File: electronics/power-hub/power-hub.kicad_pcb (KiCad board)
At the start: 2 copper layers, 120 x 70 mm, 74 parts, among them J1 24V IN, J2 ROW A, J3 ROW B, J4 ROW C, J5 ROW D, J6 ROW AUX, J7 SUPERVISOR, Q1 SUD50P06-15, U1 TPS26600PWPR, U2 TPS26600PWPR, U3 TPS26600PWPR, U4 TPS26600PWPR, U5 TPS26600PWPR

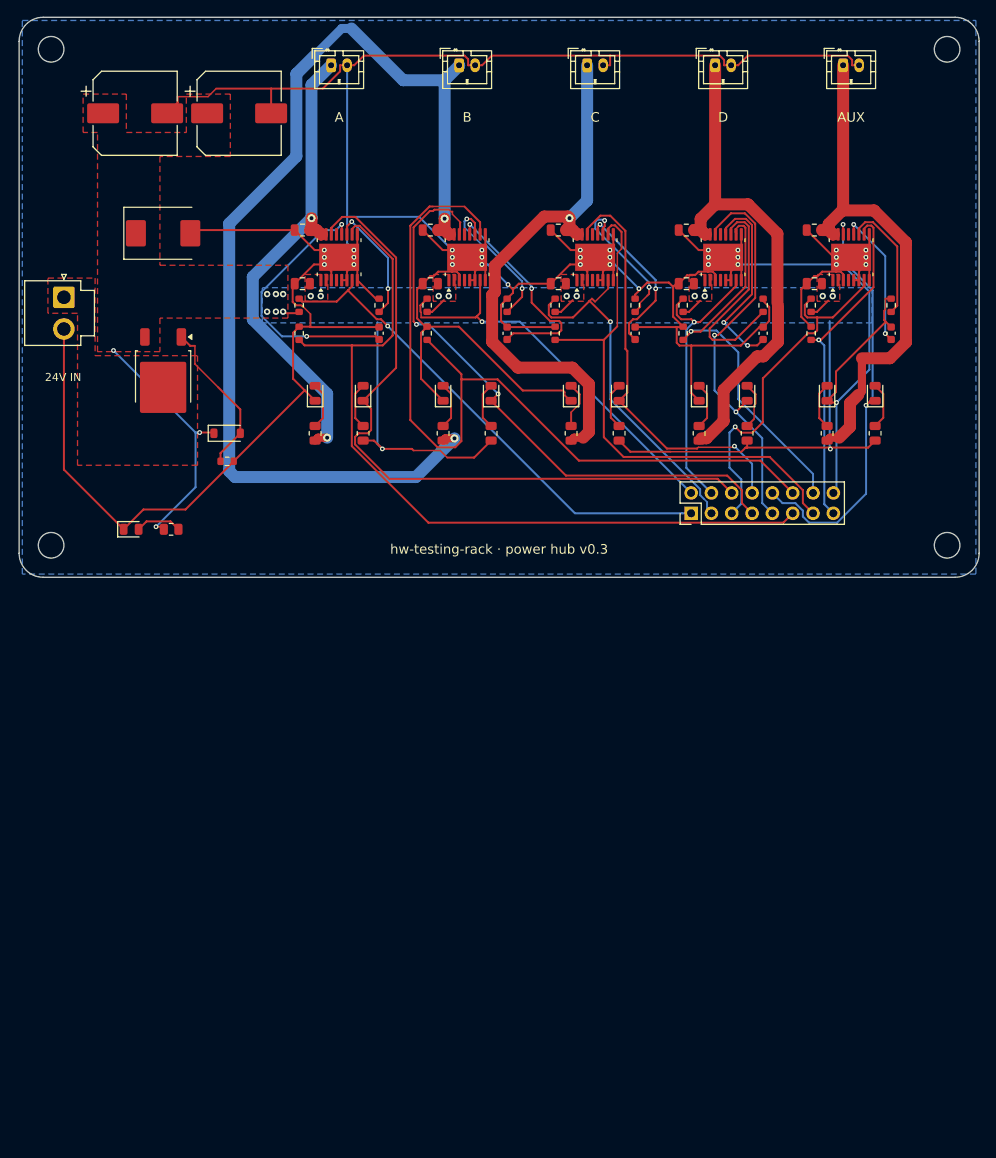
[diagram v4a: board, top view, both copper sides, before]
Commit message: Power hub v0.4: eFuses + rack controller (ESP32-S3, CAN master)
A new board for the power box: 76 x 140 mm, 2 layers, drawn around the
outline, holes, row connectors and front LEDs in config/rack.yaml.

- 24 V in on a JST VH (the brick's crimped DC cord), P-FET + TVS + bulk,
  then 4 x TPS26600 (1.6 A) to 6-pin JST PH row outputs: 24 V, GND,
  CAN_H, CAN_L, GND, POS (docs/can.md)
- every row on without firmware (SHDN held high by a 1M/150k divider from
  24 V); the controller can switch a row off (2N7002) and reads FLT and IMON
- rack controller: ESP32-S3-MINI-1, LMR51635 5 V buck (the bay node's
  layout) diode-ORed with USB-C VBUS, AMS1117; TCAN1044AV with both
  terminations of the star bus (2 x 56 ohm split, twice), PESD2CAN; POS per
  row through 10k + BAT54S clamp (survives a reversed cable)
- side-view ON / FAULT LEDs per row, 24V and CTL in the box's front wall
- autorouted; ERC 0, DRC 0, 0 unconnected, parity 0; Konnect review in
  docs/review-konnect.md (VBUS cap added; the rest per-sheet false positives)
- box re-generated for the final hole / connector / LED positions; viewer
  shows the real board; BOM carries an estimate (Standard PCBA, not quoted)
- schematic: automatic block layout for now

Co-Authored-By: Claude Opus 5.5 <noreply@anthropic.com>
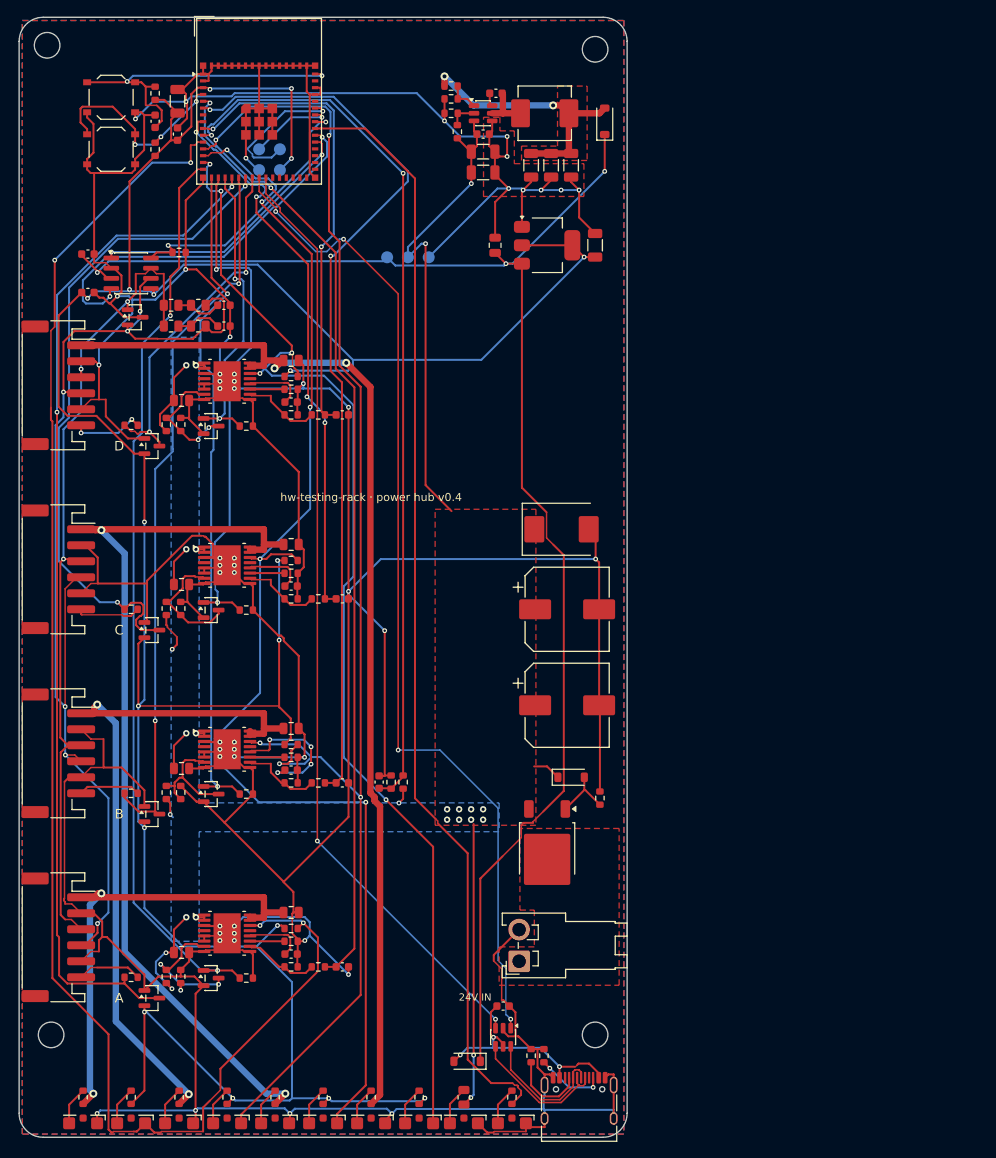
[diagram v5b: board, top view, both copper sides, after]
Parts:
- removed C15, C35: 1u, Capacitor_SMD:C_0805_2012Metric
- removed C25: 22n, Capacitor_SMD:C_0603_1608Metric
- removed D15: ON, LED_SMD:LED_0805_2012Metric
- removed D25: FAULT, LED_SMD:LED_0805_2012Metric
- removed J7: SUPERVISOR, Connector_PinHeader_2.54mm:PinHeader_2x08_P2.54mm_Vertical
- removed R15: 470k, Resistor_SMD:R_0603_1608Metric
- removed R25: 7.5k, Resistor_SMD:R_0603_1608Metric
- removed R35: 18k, Resistor_SMD:R_0603_1608Metric
- removed R45, R55: 10k, Resistor_SMD:R_0805_2012Metric
- removed U1: TPS26600PWPR, Package_SO:HTSSOP-16-1EP_4.4x5mm_P0.65mm_EP3.4x5mm_Mask2.66x2.46mm
- added C104: 10u, Capacitor_SMD:C_1206_3216Metric, F.Cu at (58.0, 16.8)
- added C105: 10u, Capacitor_SMD:C_1206_3216Metric, F.Cu at (58.0, 19.4)
- added C106: 100n, Capacitor_SMD:C_0603_1608Metric, F.Cu at (58.0, 14.6)
- added C107: 100n, Capacitor_SMD:C_0603_1608Metric, F.Cu at (59.6, 9.50)
- added C108: 22u, Capacitor_SMD:C_1206_3216Metric, F.Cu at (64.0, 18.5)
- added C109: 22u, Capacitor_SMD:C_1206_3216Metric, F.Cu at (66.5, 18.5)
- added C110: 22u, Capacitor_SMD:C_1206_3216Metric, F.Cu at (69.0, 18.5)
- added C111: 10u, Capacitor_SMD:C_0805_2012Metric, F.Cu at (59.5, 28.5)
- added C112: 22u, Capacitor_SMD:C_1206_3216Metric, F.Cu at (72.0, 28.5)
- added C113: 22u, Capacitor_SMD:C_1206_3216Metric, F.Cu at (19.8, 10.5)
- added C114: 100n, Capacitor_SMD:C_0603_1608Metric, F.Cu at (19.8, 14.6)
- added C115: 1u, Capacitor_SMD:C_0603_1608Metric, F.Cu at (17.0, 13.0)
- added C116: 100n, Capacitor_SMD:C_0603_1608Metric, F.Cu at (8.60, 29.6)
- added C117: 100n, Capacitor_SMD:C_0603_1608Metric, F.Cu at (8.60, 34.4)
- added C118: 4.7n, Capacitor_SMD:C_0603_1608Metric, F.Cu at (25.6, 36.0)
- added C119: 4.7n, Capacitor_SMD:C_0603_1608Metric, F.Cu at (25.6, 38.6)
- added C120: 1u, Capacitor_SMD:C_0603_1608Metric, F.Cu at (60.5, 123.6)
- added C3: 100n, Capacitor_SMD:C_0603_1608Metric, F.Cu at (45.0, 95.6)
- added C61: 10n, Capacitor_SMD:C_0603_1608Metric, F.Cu at (40.4, 118.7)
- added C62: 10n, Capacitor_SMD:C_0603_1608Metric, F.Cu at (40.4, 95.7)
- added C63: 10n, Capacitor_SMD:C_0603_1608Metric, F.Cu at (40.4, 72.7)
- added C64: 10n, Capacitor_SMD:C_0603_1608Metric, F.Cu at (40.4, 49.7)
- added D31: BAT54S, Package_TO_SOT_SMD:SOT-23, F.Cu at (16.6, 122.6)
- added D32: BAT54S, Package_TO_SOT_SMD:SOT-23, F.Cu at (16.6, 99.6)
- added D33: BAT54S, Package_TO_SOT_SMD:SOT-23, F.Cu at (16.6, 76.6)
- added D34: BAT54S, Package_TO_SOT_SMD:SOT-23, F.Cu at (16.6, 53.6)
- added D4: B5819W SL, Diode_SMD:D_SOD-123, F.Cu at (73.2, 13.0)
- added D5: B5819W SL, Diode_SMD:D_SOD-123, F.Cu at (56.0, 130.5)
- added D8: CTL, LED_SMD:LED_Kingbright_KPA-3010_3x2x1mm, F.Cu at (61.6, 138.8)
- added D9: PESD2CAN,215, Package_TO_SOT_SMD:SOT-23, F.Cu at (14.5, 37.5)
- added L1: 3.3u, Inductor_SMD:L_Changjiang_FXL0630, F.Cu at (65.7, 12.0)
- added Q2: 2N7002, Package_TO_SOT_SMD:SOT-23, F.Cu at (24.0, 120.1)
- added Q3: 2N7002, Package_TO_SOT_SMD:SOT-23, F.Cu at (24.0, 97.1)
- added Q4: 2N7002, Package_TO_SOT_SMD:SOT-23, F.Cu at (24.0, 74.1)
- added Q5: 2N7002, Package_TO_SOT_SMD:SOT-23, F.Cu at (24.0, 51.1)
- added R101: 10k, Resistor_SMD:R_0603_1608Metric, F.Cu at (14.0, 120.0)
- added R102: 10k, Resistor_SMD:R_0603_1608Metric, F.Cu at (14.0, 97.0)
- added R103: 10k, Resistor_SMD:R_0603_1608Metric, F.Cu at (14.0, 74.0)
- added R104: 10k, Resistor_SMD:R_0603_1608Metric, F.Cu at (14.0, 51.0)
- added R205: 1M, Resistor_SMD:R_0603_1608Metric, F.Cu at (54.8, 14.3)
- added R206: 100k, Resistor_SMD:R_0603_1608Metric, F.Cu at (54.0, 12.0)
- added R207: 120k, Resistor_SMD:R_0603_1608Metric, F.Cu at (54.0, 8.60)
- added R208: 22k, Resistor_SMD:R_0603_1608Metric, F.Cu at (54.0, 10.2)
- added R209: 10k, Resistor_SMD:R_0603_1608Metric, F.Cu at (17.0, 9.50)
- added R210: 10k, Resistor_SMD:R_0603_1608Metric, F.Cu at (17.0, 16.5)
- added R211: 330, Resistor_SMD:R_0603_1608Metric, F.Cu at (61.6, 135.0)
- added R212: 5.1k, Resistor_SMD:R_0603_1608Metric, F.Cu at (64.0, 129.8)
- added R213: 5.1k, Resistor_SMD:R_0603_1608Metric, F.Cu at (65.6, 129.8)
- added R214: 10k, Resistor_SMD:R_0603_1608Metric, F.Cu at (20.0, 29.4)
- added R215: 62, Resistor_SMD:R_0805_2012Metric, F.Cu at (19.0, 36.0)
- added R216: 62, Resistor_SMD:R_0805_2012Metric, F.Cu at (22.4, 36.0)
- added R217: 62, Resistor_SMD:R_0805_2012Metric, F.Cu at (19.0, 38.6)
- added R218: 62, Resistor_SMD:R_0805_2012Metric, F.Cu at (22.4, 38.6)
- added R3: 100k, Resistor_SMD:R_0603_1608Metric, F.Cu at (48.0, 95.6)
- added R4: 10k, Resistor_SMD:R_0603_1608Metric, F.Cu at (46.5, 95.6)
- added R61: 1k, Resistor_SMD:R_0603_1608Metric, F.Cu at (37.4, 118.7)
- added R62: 1k, Resistor_SMD:R_0603_1608Metric, F.Cu at (37.4, 95.7)
- added R63: 1k, Resistor_SMD:R_0603_1608Metric, F.Cu at (37.4, 72.7)
- added R64: 1k, Resistor_SMD:R_0603_1608Metric, F.Cu at (37.4, 49.7)
- added R71: 150k, Resistor_SMD:R_0603_1608Metric, F.Cu at (20.2, 119.9)
- added R72: 150k, Resistor_SMD:R_0603_1608Metric, F.Cu at (20.2, 96.9)
- added R73: 150k, Resistor_SMD:R_0603_1608Metric, F.Cu at (20.2, 73.9)
- added R74: 150k, Resistor_SMD:R_0603_1608Metric, F.Cu at (20.2, 50.9)
- added R81: 100k, Resistor_SMD:R_0603_1608Metric, F.Cu at (28.4, 120.1)
- added R82: 100k, Resistor_SMD:R_0603_1608Metric, F.Cu at (28.4, 97.1)
- added R83: 100k, Resistor_SMD:R_0603_1608Metric, F.Cu at (28.4, 74.1)
- added R84: 100k, Resistor_SMD:R_0603_1608Metric, F.Cu at (28.4, 51.1)
- added R91: 100k, Resistor_SMD:R_0603_1608Metric, F.Cu at (34.0, 113.9)
- added R92: 100k, Resistor_SMD:R_0603_1608Metric, F.Cu at (34.0, 90.9)
- added R93: 100k, Resistor_SMD:R_0603_1608Metric, F.Cu at (34.0, 67.9)
- added R94: 100k, Resistor_SMD:R_0603_1608Metric, F.Cu at (34.0, 44.9)
- added SW1: RESET, Button_Switch_SMD:SW_Push_1P1T_XKB_TS-1187A, F.Cu at (11.5, 10.0)
- added SW2: BOOT, Button_Switch_SMD:SW_Push_1P1T_XKB_TS-1187A, F.Cu at (11.5, 16.5)
- added TP1: U0TX, TestPoint:TestPoint_Pad_D1.5mm, B.Cu at (30.0, 16.5)
- added TP2: U0RX, TestPoint:TestPoint_Pad_D1.5mm, B.Cu at (32.6, 16.5)
- added TP3: GND, TestPoint:TestPoint_Pad_D1.5mm, B.Cu at (30.0, 19.1)
- added TP4: +3V3, TestPoint:TestPoint_Pad_D1.5mm, B.Cu at (32.6, 19.1)
- added TP5: +5V, TestPoint:TestPoint_Pad_D1.5mm, B.Cu at (46.0, 30.0)
- added TP6: +24V, TestPoint:TestPoint_Pad_D1.5mm, B.Cu at (48.6, 30.0)
- added TP7: GND, TestPoint:TestPoint_Pad_D1.5mm, B.Cu at (51.2, 30.0)
- added U11: TPS26600PWPR, Package_SO:HTSSOP-16-1EP_4.4x5mm_P0.65mm_EP3.4x5mm_Mask2.66x2.46mm, F.Cu at (26.0, 114.5)
- added U12: TPS26600PWPR, Package_SO:HTSSOP-16-1EP_4.4x5mm_P0.65mm_EP3.4x5mm_Mask2.66x2.46mm, F.Cu at (26.0, 91.5)
- added U13: TPS26600PWPR, Package_SO:HTSSOP-16-1EP_4.4x5mm_P0.65mm_EP3.4x5mm_Mask2.66x2.46mm, F.Cu at (26.0, 68.5)
- added U14: TPS26600PWPR, Package_SO:HTSSOP-16-1EP_4.4x5mm_P0.65mm_EP3.4x5mm_Mask2.66x2.46mm, F.Cu at (26.0, 45.5)
- added U6: TCAN1044AV, Package_SO:SOIC-8_3.9x4.9mm_P1.27mm, F.Cu at (14.0, 32.0)
- D11, D12, D13, D14, D21, D22, D23, D24, D3: footprint LED_SMD:LED_0805_2012Metric -> LED_SMD:LED_Kingbright_KPA-3010_3x2x1mm
- J1: footprint Connector_JST:JST_VH_B2P-VH_1x02_P3.96mm_Vertical -> Connector_JST:JST_VH_S2P-VH_1x02_P3.96mm_Horizontal
- J2, J3, J4, J5: footprint Connector_JST:JST_PH_B2B-PH-K_1x02_P2.00mm_Vertical -> Connector_JST:JST_PH_S6B-PH-SM4-TB_1x06-1MP_P2.00mm_Horizontal
- J6: value ROW AUX -> USB; footprint Connector_JST:JST_PH_B2B-PH-K_1x02_P2.00mm_Vertical -> Connector_USB:USB_C_Receptacle_HRO_TYPE-C-31-M-12
- R11, R12, R13, R14: value 470k -> 1M
- R41, R42, R43, R44: footprint Resistor_SMD:R_0805_2012Metric -> Resistor_SMD:R_0603_1608Metric
- R51, R52, R53, R54: value 10k -> 680; footprint Resistor_SMD:R_0805_2012Metric -> Resistor_SMD:R_0603_1608Metric
- U2: value TPS26600PWPR -> LMR51635YDDCR; footprint Package_SO:HTSSOP-16-1EP_4.4x5mm_P0.65mm_EP3.4x5mm_Mask2.66x2.46mm -> Package_TO_SOT_SMD:TSOT-23-6
- U3: value TPS26600PWPR -> AMS1117-3.3; footprint Package_SO:HTSSOP-16-1EP_4.4x5mm_P0.65mm_EP3.4x5mm_Mask2.66x2.46mm -> Package_TO_SOT_SMD:SOT-223-3_TabPin2
- U4: value TPS26600PWPR -> ESP32-S3-MINI-1-N8; footprint Package_SO:HTSSOP-16-1EP_4.4x5mm_P0.65mm_EP3.4x5mm_Mask2.66x2.46mm -> RF_Module:ESP32-S2-MINI-1
- U5: value TPS26600PWPR -> USBLC6-2SC6; footprint Package_SO:HTSSOP-16-1EP_4.4x5mm_P0.65mm_EP3.4x5mm_Mask2.66x2.46mm -> Package_TO_SOT_SMD:SOT-23-6
- moved J6 134.7 mm to (70.0, 136.6)
- moved J2 114.2 mm to (4.90, 115.0), turned to -90 degrees
- moved U5 106.8 mm to (60.5, 127.5), turned to -90 degrees
- moved J1 100.6 mm to (62.5, 118.0), turned to 90 degrees
- moved D14 100.5 mm to (44.0, 138.8), turned to 180 degrees
- moved D24 100.5 mm to (50.0, 138.8), turned to 180 degrees
- moved J3 99.5 mm to (4.90, 92.0), turned to -90 degrees
- moved D13 98.9 mm to (32.0, 138.8), turned to 180 degrees
- moved D23 98.9 mm to (38.0, 138.8), turned to 180 degrees
- moved D12 97.5 mm to (20.0, 138.8), turned to 180 degrees
- moved D22 97.5 mm to (26.0, 138.8), turned to 180 degrees
- moved D11 96.2 mm to (8.00, 138.8), turned to 180 degrees
- moved D21 96.2 mm to (14.0, 138.8), turned to 180 degrees
- moved R44 92.6 mm to (44.0, 135.0)
- moved R54 92.6 mm to (50.0, 135.0)
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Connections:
- R11 pad 2: SHDN_A -> /Outputs/SHDN_A
- R12 pad 2: SHDN_B -> /Outputs/SHDN_B
- R13 pad 2: SHDN_C -> /Outputs/SHDN_C
- R14 pad 2: SHDN_D -> /Outputs/SHDN_D
- R31 pad 1: IMON_A -> /Outputs/IMON_A
- R32 pad 1: IMON_B -> /Outputs/IMON_B
- R33 pad 1: IMON_C -> /Outputs/IMON_C
- R34 pad 1: IMON_D -> /Outputs/IMON_D
- R51 pad 1: +24V -> +3V3
- R52 pad 1: +24V -> +3V3
- R53 pad 1: +24V -> +3V3
- R54 pad 1: +24V -> +3V3
- U2 pad 1: +24V -> /Controller/BUCK_FB
- U2 pad 2: +24V -> /Controller/BUCK_EN
- U2 pad 3: GND -> +24V
- U2 pad 4: unconnected-(U2-NC-Pad4) -> GND
- U2 pad 5: GND -> /Controller/BUCK_SW
- U2 pad 6: GND -> /Controller/BUCK_CB
- U3 pad 1: +24V -> GND
- U3 pad 2: +24V -> +3V3
- U3 pad 3: GND -> +5V
- U4 pad 1: +24V -> GND
- U4 pad 10: IMON_D -> VSENSE
- U4 pad 11: /Outputs/ILIM_D -> FLT_A
- U4 pad 12: /Outputs/DVDT_D -> FLT_B
- U4 pad 13: unconnected-(U4-NC-Pad13) -> FLT_C
- U4 pad 15: /Outputs/ROW_D -> ROW_OFF_A
- U4 pad 16: /Outputs/ROW_D -> ROW_OFF_B
- U4 pad 17: GND -> ROW_OFF_C
- U4 pad 2: +24V -> GND
- U4 pad 3: GND -> +3V3
- U4 pad 4: unconnected-(U4-NC-Pad4) -> /Controller/BOOT
- U4 pad 5: GND -> ADC_IMON_A
- U4 pad 6: GND -> ADC_IMON_B
- U4 pad 7: SHDN_D -> unconnected-(U4-IO3-Pad7)
- U4 pad 8: GND -> ADC_IMON_C
- U4 pad 9: GND -> ADC_IMON_D
- U5 pad 1: +24V -> /Controller/USB_DN
- U5 pad 2: +24V -> GND
- U5 pad 3: GND -> /Controller/USB_DP
- U5 pad 4: unconnected-(U5-NC-Pad4) -> /Controller/USB_CONN_DP
- U5 pad 5: GND -> /Controller/VBUS
- U5 pad 6: GND -> /Controller/USB_CONN_DN
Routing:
- net +3V3: track 0.00 -> 391.1 mm, vias 0 -> 18
- net GND: track 551.6 -> 937.8 mm, vias 33 -> 51
- net +5V: track 0.00 -> 190.2 mm, vias 0 -> 3
- net CAN_L: track 0.00 -> 139.3 mm, vias 0 -> 6
- net /Controller/CTL_LED: track 0.00 -> 138.4 mm
- net POS_A: track 0.00 -> 128.2 mm, vias 0 -> 2
- net /Controller/USB_DN: track 0.00 -> 126.7 mm, vias 0 -> 4
- net ADC_IMON_A: track 0.00 -> 120.3 mm, vias 0 -> 2
- net /Controller/USB_DP: track 0.00 -> 118.2 mm, vias 0 -> 2
- net ROW_OFF_A: track 0.00 -> 114.6 mm, vias 0 -> 2
- net ADC_IMON_B: track 0.00 -> 113.2 mm, vias 0 -> 2
- net VSENSE: track 0.00 -> 110.9 mm, vias 0 -> 2
- net FLT_C: track 52.5 -> 160.6 mm, vias 1 -> 5
- net IMON_B: track 106.2 -> 0.00 mm
- net CAN_H: track 0.00 -> 104.8 mm, vias 0 -> 3
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- added copper zone on F.Cu, net /Controller/+5V_BUCK
- added copper zone on F.Cu, net GND
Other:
- board size 120 x 70 mm -> 76 x 140 mm
- board text added: "hw-testing-rack · power hub v0.4"
- board text removed: "AUX"
- board text removed: "hw-testing-rack · power hub v0.3"

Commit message: Power hub v0.5: USB-C PD input (AP33772S), 4 layers, rows off until enabled
The rack now runs from one USB PD 3.1 charger instead of the GST60A24 brick.

Hub v0.5 (76 x 140 mm, 4 layers, In1 GND, In2 VRACK/+3V3):
* AP33772S sink: 20 V at power-up (VSEL 39k), 28 V EPR on the controller's
  request, never 36/48 V; 5 mOhm Kelvin shunt, back-to-back IRF7842 switch,
  SMAJ30A TVS, NTC by the switch, interrupt and I2C to the ESP32-S3.
* USB4105 5 A receptacle; the controller's buck runs from VBUS (5-28 V),
  ahead of the switch.
* Every row's TPS26600 is off until the controller drives ROW_EN (SHDN pulled
  low); IMON per row; front PD LED.
* ERC 0, DRC 0 errors, 0 unconnected, parity 0; 146 3D models, 0 stand-ins.

Power box: 84 x 148 x 35 mm, hub only (no brick, no cradles), rear USB-C
cut-out, lid on corner lugs.  Viewer, BOM (charger + 5 A e-marked cable,
4-layer JLC estimate) and docs (power, mechanical, cabling, assembly,
electronics) follow.

Co-Authored-By: Claude Opus 5.5 <noreply@anthropic.com>
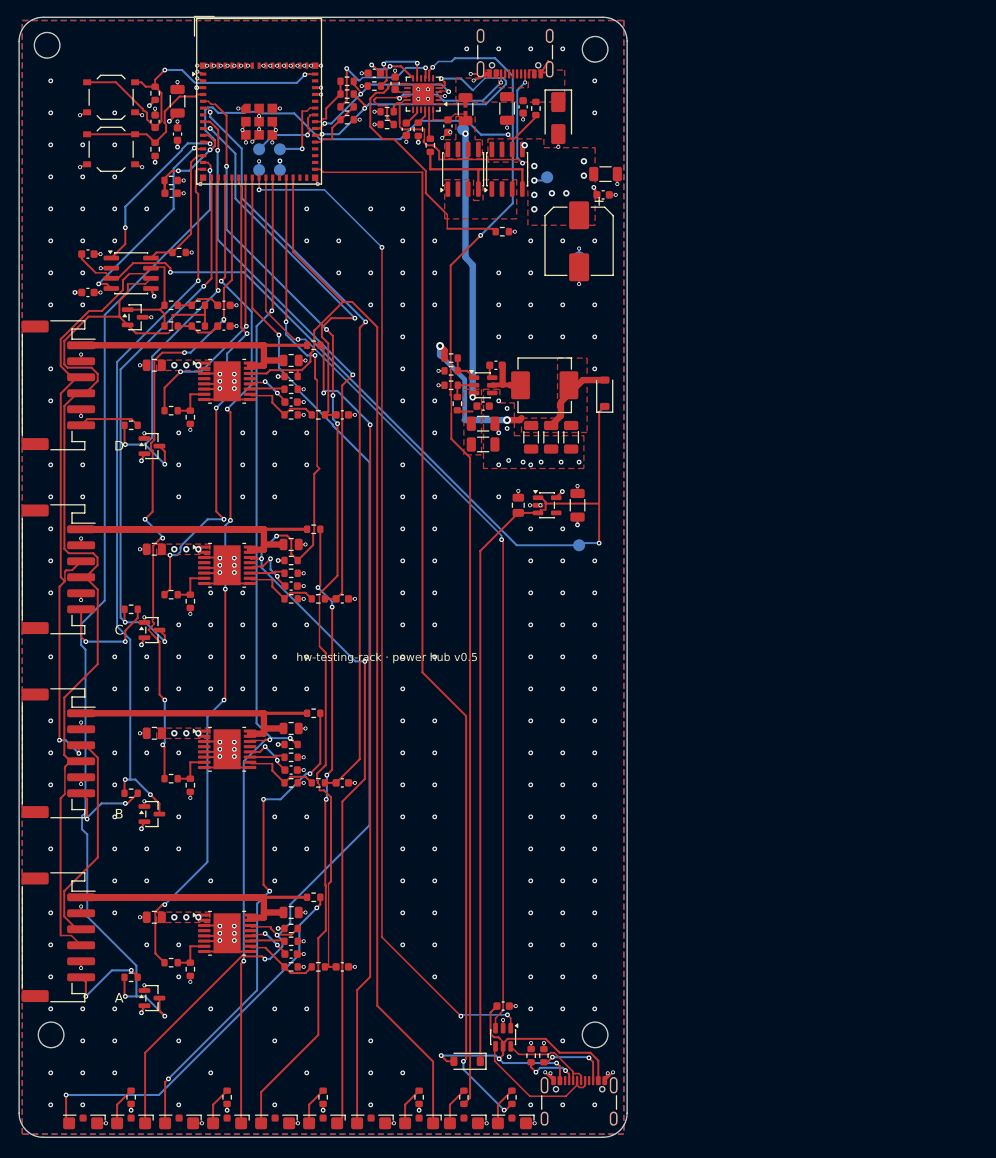
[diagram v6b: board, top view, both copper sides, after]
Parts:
- removed D2: SMCJ33A, Diode_SMD:D_SMC
- removed Q3, Q4, Q5: 2N7002, Package_TO_SOT_SMD:SOT-23
- added C10: 100n, Capacitor_SMD:C_0603_1608Metric, F.Cu at (73.0, 22.2)
- added C4: 1u, Capacitor_SMD:C_0603_1608Metric, F.Cu at (53.6, 13.6)
- added C5: 1u, Capacitor_SMD:C_0603_1608Metric, F.Cu at (48.4, 14.0)
- added C6: 100n, Capacitor_SMD:C_0603_1608Metric, F.Cu at (44.4, 7.00)
- added C7: 100n, Capacitor_SMD:C_0603_1608Metric, F.Cu at (47.0, 8.25)
- added C8: 100u/50V, Capacitor_SMD:CP_Elec_8x10, F.Cu at (70.0, 28.0)
- added C9: 10u, Capacitor_SMD:C_1206_3216Metric, F.Cu at (73.3, 19.6)
- added R5: 5.1k, Resistor_SMD:R_0603_1608Metric, F.Cu at (46.0, 11.8)
- added R6: 5.1k, Resistor_SMD:R_0603_1608Metric, F.Cu at (46.0, 13.4)
- added R7: 39k, Resistor_SMD:R_0603_1608Metric, F.Cu at (44.4, 8.60)
- added R8: 6.2k, Resistor_SMD:R_0603_1608Metric, F.Cu at (51.4, 16.0)
- added R9: 200, Resistor_SMD:R_0603_1608Metric, F.Cu at (49.9, 14.0)
- added TH1: 10k NTC, Resistor_SMD:R_0603_1608Metric, F.Cu at (60.4, 26.8)
- added TP8: PD_VCC, TestPoint:TestPoint_Pad_D1.5mm, B.Cu at (55.5, 14.0)
- added U1: AP33772SDKZ-13-FA02, Package_DFN_QFN:QFN-24-1EP_4x4mm_P0.5mm_EP2.7x2.7mm, F.Cu at (50.5, 9.60)
- C1: value 220u/50V -> 10u; footprint Capacitor_SMD:CP_Elec_10x10 -> Capacitor_SMD:C_1206_3216Metric
- C2: value 220u/50V -> 100n; footprint Capacitor_SMD:CP_Elec_10x10 -> Capacitor_SMD:C_0603_1608Metric
- D1: value BZT52C12 -> SMAJ30A; footprint Diode_SMD:D_SOD-123 -> Diode_SMD:D_SMA
- D3: value 24V -> PD
- J1: value 24V IN -> PD IN; footprint Connector_JST:JST_VH_S2P-VH_1x02_P3.96mm_Horizontal -> Connector_USB:USB_C_Receptacle_GCT_USB4105-xx-A_16P_TopMnt_Horizontal
- J6: footprint Connector_USB:USB_C_Receptacle_HRO_TYPE-C-31-M-12 -> Connector_USB:USB_C_Receptacle_GCT_USB4105-xx-A_16P_TopMnt_Horizontal
- Q1: value SUD50P06-15 -> IRF7842TRPBF; footprint Package_TO_SOT_SMD:TO-252-2 -> Package_SO:SOIC-8_3.9x4.9mm_P1.27mm
- Q2: value 2N7002 -> IRF7842TRPBF; footprint Package_TO_SOT_SMD:SOT-23 -> Package_SO:SOIC-8_3.9x4.9mm_P1.27mm
- R1: value 100k -> 5m; footprint Resistor_SMD:R_0603_1608Metric -> bench:R_1206_3216Metric_Kelvin
- R11: value 1M -> 15k
- R12: value 1M -> 27k
- R13, R14: value 1M -> 4.7k
- R2: value 10k -> 1k; footprint Resistor_SMD:R_0805_2012Metric -> Resistor_SMD:R_0603_1608Metric
- R205: value 1M -> 100k
- R206: value 100k -> 47k
- R215, R216, R217, R218: value 62 -> 56; footprint Resistor_SMD:R_0805_2012Metric -> Resistor_SMD:R_0603_1608Metric
- R71, R72, R73, R74: value 150k -> 100k
- R81, R82, R83, R84: value 100k -> 10k
- TP6: value +24V -> VRACK
- U3: value AMS1117-3.3 -> AP2112K-3.3TRG1; footprint Package_TO_SOT_SMD:SOT-223-3_TabPin2 -> Package_TO_SOT_SMD:SOT-23-5
- moved J1 114.6 mm to (62.0, 3.40), turned to 180 degrees
- moved R11 111.0 mm to (41.0, 11.2), turned to 0 degrees
- moved Q2 107.7 mm to (61.0, 19.0), turned to 90 degrees
- moved R44 94.3 mm to (36.8, 41.0), turned to 0 degrees
- moved R1 87.7 mm to (55.8, 11.5), turned to -90 degrees
- moved R12 87.1 mm to (41.0, 12.8), turned to 0 degrees
- moved R3 85.8 mm to (64.6, 11.4), turned to -90 degrees
- moved Q1 85.6 mm to (55.5, 19.0), turned to 90 degrees
- moved D1 82.4 mm to (67.4, 12.6), turned to -90 degrees
- moved R4 80.1 mm to (19.0, 20.4), turned to 0 degrees
- moved C3 78.1 mm to (19.0, 22.0), turned to 0 degrees
- moved C1 75.0 mm to (61.0, 11.4), turned to -90 degrees
- moved R43 71.2 mm to (36.8, 64.0), turned to 0 degrees
- moved R13 69.7 mm to (41.0, 8.00), turned to 0 degrees
- moved C2 63.0 mm to (63.0, 11.2), turned to -90 degrees
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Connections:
- net /Controller/VBUS renamed /Controller/USB_VBUS
- net /Input/PWR_LED renamed /Input/PD_LED_A
- net VSENSE renamed VBUS_SENSE
- C1 pad 1: +24V -> /Input/PD_VBUS
- C104 pad 1: +24V -> PD_VCC
- C105 pad 1: +24V -> PD_VCC
- C106 pad 1: +24V -> PD_VCC
- C11 pad 1: +24V -> VRACK
- C12 pad 1: +24V -> VRACK
- C13 pad 1: +24V -> VRACK
- C14 pad 1: +24V -> VRACK
- C2 pad 1: +24V -> /Input/PD_VBUS
- D1 pad 1: +24V -> /Input/PD_VBUS
- D1 pad 2: /Input/Q1_GATE -> GND
- Q1 pad 1: /Input/Q1_GATE -> /Input/PD_SRC
- Q1 pad 2: /Input/VIN_RAW -> /Input/PD_SRC
- Q1 pad 3: +24V -> /Input/PD_SRC
- Q2 pad 1: ROW_OFF_A -> /Input/PD_SRC
- Q2 pad 2: GND -> /Input/PD_SRC
- Q2 pad 3: /Outputs/SHDN_A -> /Input/PD_SRC
- R1 pad 1: /Input/Q1_GATE -> /Input/PD_VBUS
- R1 pad 2: GND -> /Input/PD_ISENP
- R11 pad 1: +24V -> /Input/PD_INT5
- R11 pad 2: /Outputs/SHDN_A -> PD_INT
- R12 pad 1: +24V -> PD_INT
- R12 pad 2: /Outputs/SHDN_B -> GND
- R13 pad 1: +24V -> I2C_PU
- R13 pad 2: /Outputs/SHDN_C -> PD_SDA
- R14 pad 1: +24V -> I2C_PU
- R14 pad 2: /Outputs/SHDN_D -> PD_SCL
- R2 pad 1: +24V -> /Input/PD_LED
- R205 pad 1: +24V -> PD_VCC
- R3 pad 1: +24V -> /Input/PD_VBUS
- R81 pad 1: ROW_OFF_A -> ROW_EN_A
- R81 pad 2: GND -> /Outputs/SHDN_A
- R82 pad 1: ROW_OFF_B -> ROW_EN_B
- R82 pad 2: GND -> /Outputs/SHDN_B
- R83 pad 1: ROW_OFF_C -> ROW_EN_C
- R83 pad 2: GND -> /Outputs/SHDN_C
- R84 pad 1: ROW_OFF_D -> ROW_EN_D
- R84 pad 2: GND -> /Outputs/SHDN_D
- TP6 pad 1: +24V -> VRACK
- U11 pad 1: +24V -> VRACK
- U11 pad 2: +24V -> VRACK
- U12 pad 1: +24V -> VRACK
- U12 pad 2: +24V -> VRACK
- U13 pad 1: +24V -> VRACK
- U13 pad 2: +24V -> VRACK
- U14 pad 1: +24V -> VRACK
- U14 pad 2: +24V -> VRACK
- U2 pad 3: +24V -> PD_VCC
- U3 pad 1: GND -> +5V
- U3 pad 2: +3V3 -> GND
- U4 pad 11: FLT_A -> /Controller/CAN_TXD
- U4 pad 12: FLT_B -> /Controller/CAN_RXD
- U4 pad 13: FLT_C -> /Controller/CAN_STB
- U4 pad 14: FLT_D -> POS_A
- U4 pad 15: ROW_OFF_A -> POS_B
- U4 pad 16: ROW_OFF_B -> POS_C
- U4 pad 17: ROW_OFF_C -> POS_D
- U4 pad 18: ROW_OFF_D -> ROW_EN_A
- U4 pad 19: POS_A -> ROW_EN_B
- U4 pad 20: POS_B -> ROW_EN_C
- U4 pad 21: POS_C -> ROW_EN_D
- U4 pad 22: POS_D -> FLT_A
- U4 pad 25: unconnected-(U4-IO21-Pad25) -> FLT_B
- U4 pad 27: unconnected-(U4-IO47-Pad27) -> FLT_C
- U4 pad 28: unconnected-(U4-IO33-Pad28) -> FLT_D
- U4 pad 31: unconnected-(U4-IO35-Pad31) -> /Controller/CTL_LED
- U4 pad 35: /Controller/CAN_TXD -> PD_INT
- U4 pad 36: /Controller/CAN_RXD -> PD_SCL
- U4 pad 37: /Controller/CTL_LED -> PD_SDA
- U4 pad 38: /Controller/CAN_STB -> I2C_PU
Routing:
- net GND: track 937.8 -> 149.0 mm, vias 51 -> 404
- net +3V3: track 391.1 -> 20.3 mm, vias 18 -> 22
- net +24V: track 149.4 -> 0.00 mm, vias 25 -> 0
- net /Input/PD_LED: track 0.00 -> 146.0 mm, vias 0 -> 2
- net ROW_OFF_A: track 114.6 -> 0.00 mm, vias 2 -> 0
- net ROW_EN_A: track 0.00 -> 105.9 mm, vias 0 -> 6
- net /Outputs/ROW_D: track 135.9 -> 35.6 mm, vias 2 -> 0
- net /Outputs/ON_D: track 4.80 -> 101.9 mm, vias 0 -> 2
- net ROW_EN_B: track 0.00 -> 84.9 mm, vias 0 -> 6
- net ROW_OFF_B: track 84.4 -> 0.00 mm, vias 2 -> 0
- net /Outputs/ON_C: track 4.80 -> 78.8 mm, vias 0 -> 4
- net ROW_OFF_C: track 64.6 -> 0.00 mm, vias 2 -> 0
- net ROW_EN_C: track 0.00 -> 59.4 mm, vias 0 -> 4
- net /Outputs/ROW_C: track 114.3 -> 56.8 mm, vias 2 -> 0
- net /Outputs/ON_B: track 4.80 -> 61.5 mm, vias 0 -> 4
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- added copper zone on In2.Cu, net +3V3
- added copper zone on F.Cu, net /Input/PD_SRC
- added copper zone on F.Cu, net /Input/PD_VBUS
- added copper zone on In1.Cu, net GND
- added copper zone on F.Cu, net PD_VCC
- added copper zone on F.Cu, net VRACK
- added copper zone on In2.Cu, net VRACK
- removed copper zone on B.Cu, net +24V
- removed copper zone on F.Cu, net +24V
- removed copper zone on F.Cu, net /Input/VIN_RAW
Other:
- copper layers 2 -> 4
- board text added: "hw-testing-rack · power hub v0.5"
- board text removed: "24V IN"
- board text removed: "hw-testing-rack · power hub v0.4"

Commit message: CAN transceiver: TCAN1462V (signal improvement) on the hub and the bay node
Same SOIC-8 pinout as the TCAN1044AV (VIO on pin 5, STB on pin 8), so the
footprint, placement and routing are unchanged: the regenerated PCBs keep
every track and via, only U6 / U11's value and fields change.  Signal
improvement (CiA 601-4, ISO 11898-2:2024 set C) damps the ringing of the
star's open branch ends; the termination (56 ohm at the hub) stays.

* catalog: TCAN1462VDRQ1 (C7399456, no LCSC stock on 2026-10-18), with the
  TCAN1044AVDRQ1 (C3234993) and NXP TJA1462AT/0Z (C3234095) as alternates;
  CPL rotation for all three.
* BOM: the board BOMs' alternates now show in the rack BOM notes; JLC
  estimates +$0.54 per board.
* docs/can.md: why the star is fine at 250 kbit/s and what SIC adds, with
  sources (TI SLLSFF2B, SLLA581A; CiA bit-timing table; NXP TJA1462).
* Both boards: ERC 0, DRC 0 errors, 0 unconnected, parity 0; 3D 0 stand-ins.

Co-Authored-By: Claude Opus 5.5 <noreply@anthropic.com>
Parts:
- U6: value TCAN1044AV -> TCAN1462V
